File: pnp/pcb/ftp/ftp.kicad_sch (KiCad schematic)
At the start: 84 parts, among them J1 Conn_01x02_Male

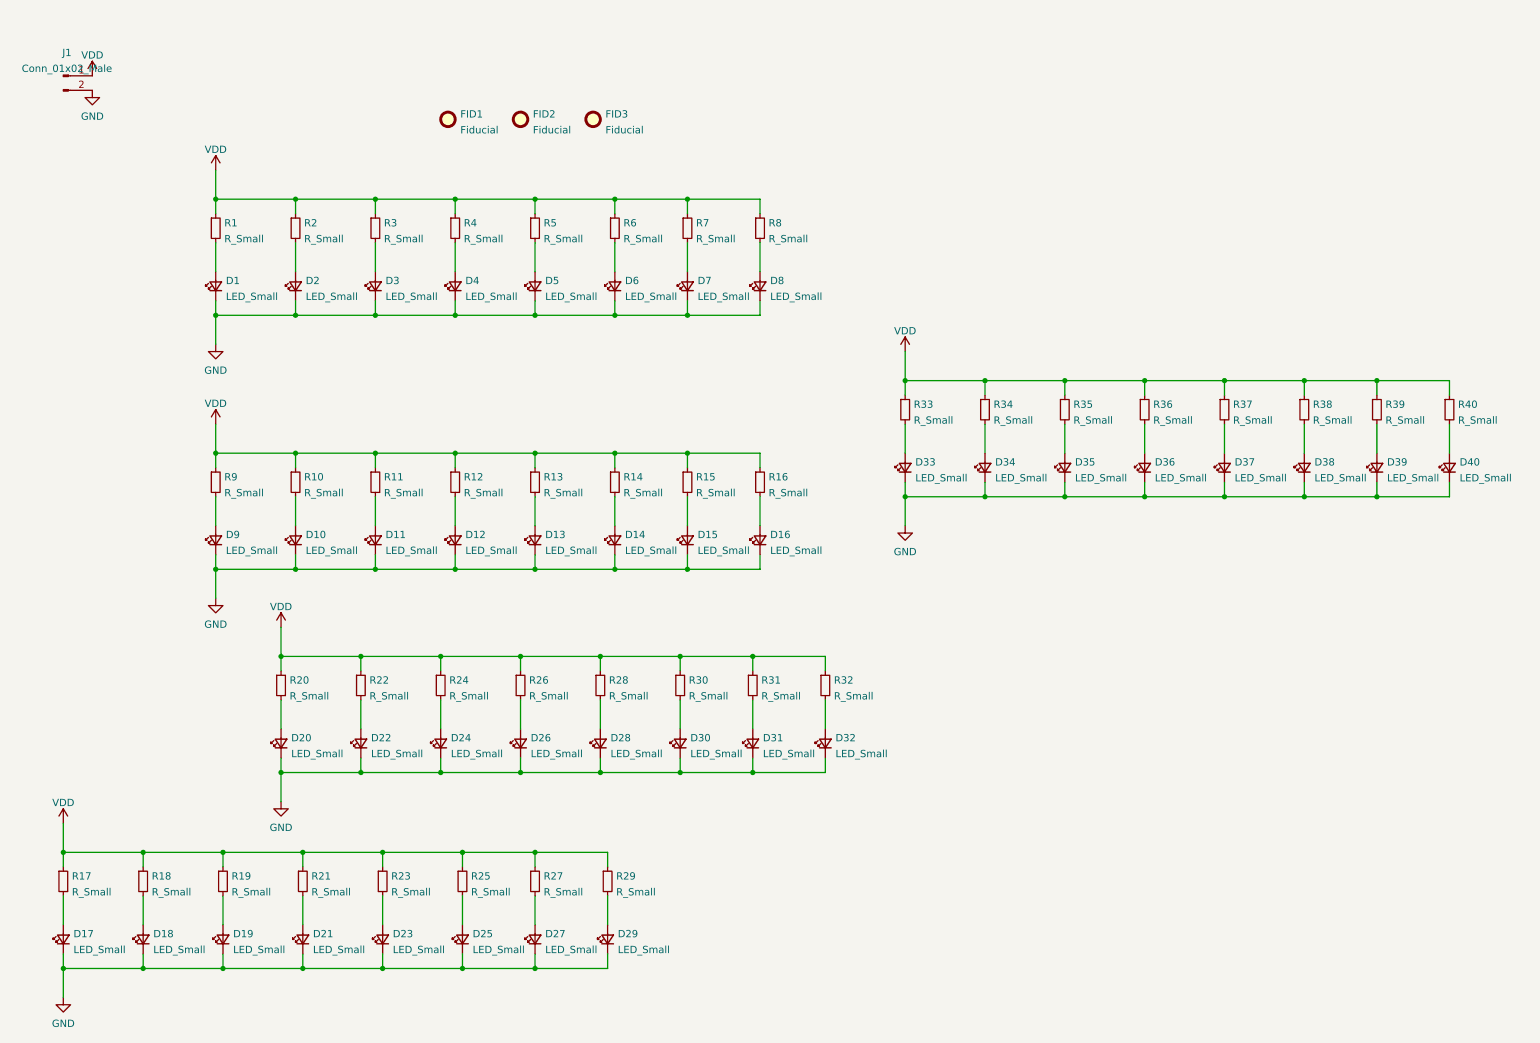
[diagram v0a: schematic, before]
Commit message: Update PCBs to KiCAD 8
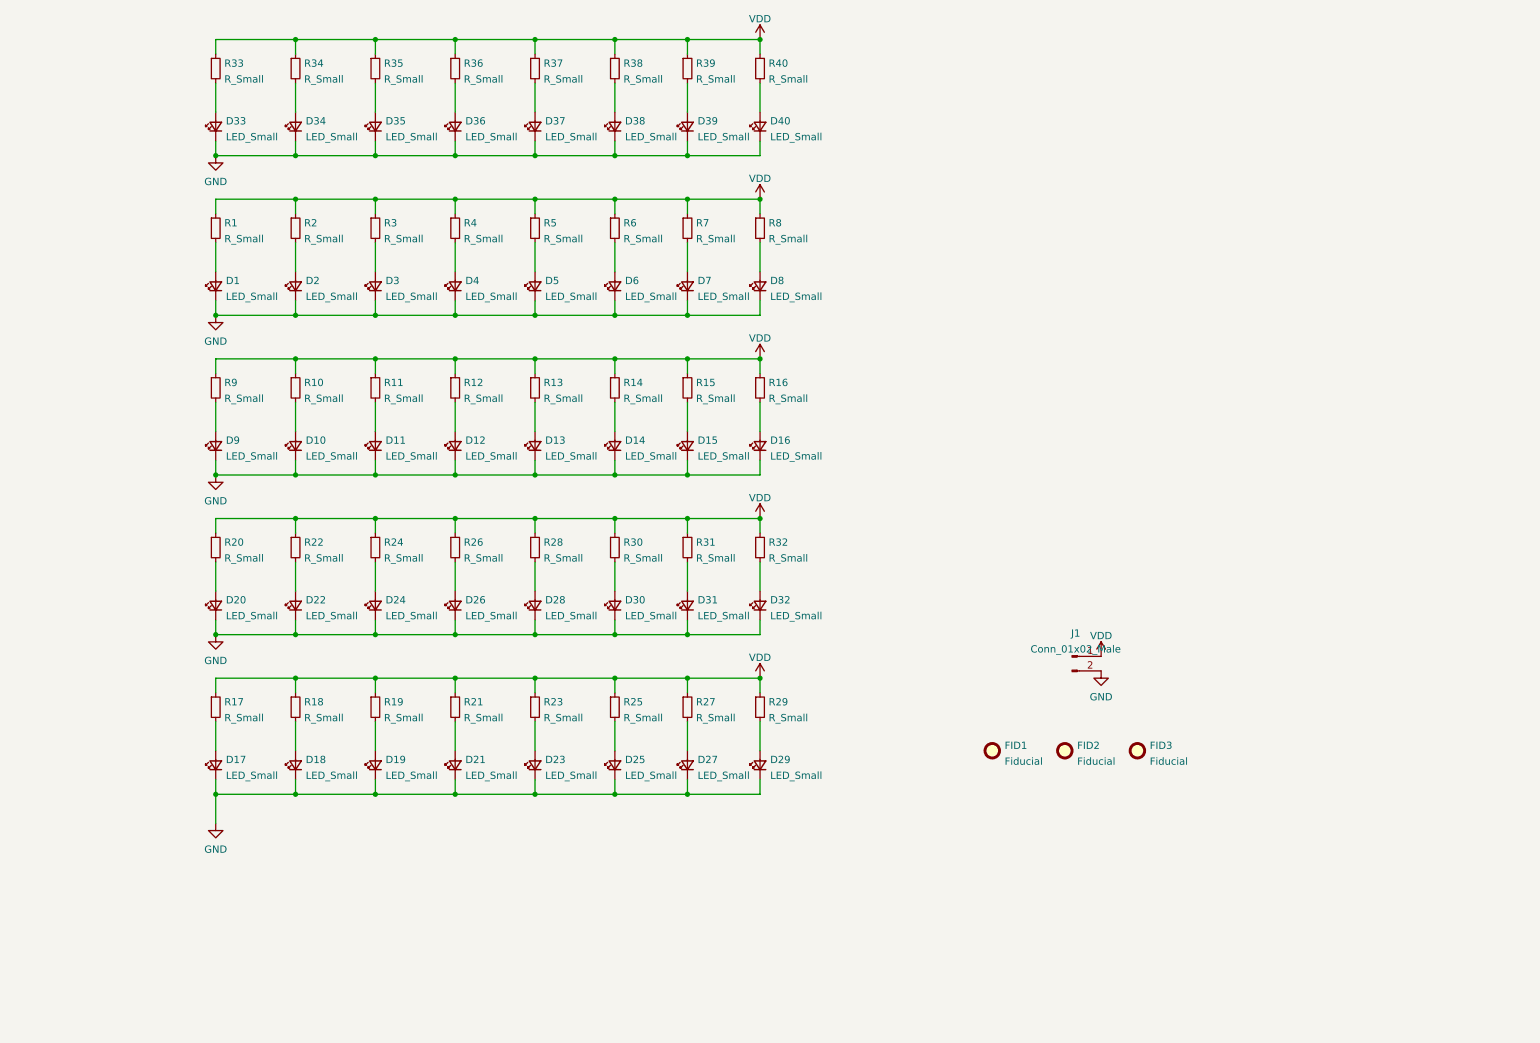
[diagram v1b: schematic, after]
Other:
- moved on the sheet: D10, D11, D12, D13, D14, D15, D16, D17, D18, D19, D20, D21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

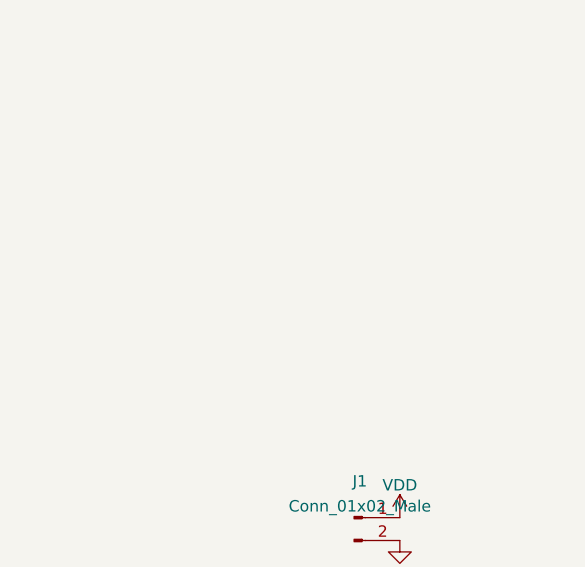
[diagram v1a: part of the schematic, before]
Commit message: Fix mounting holes
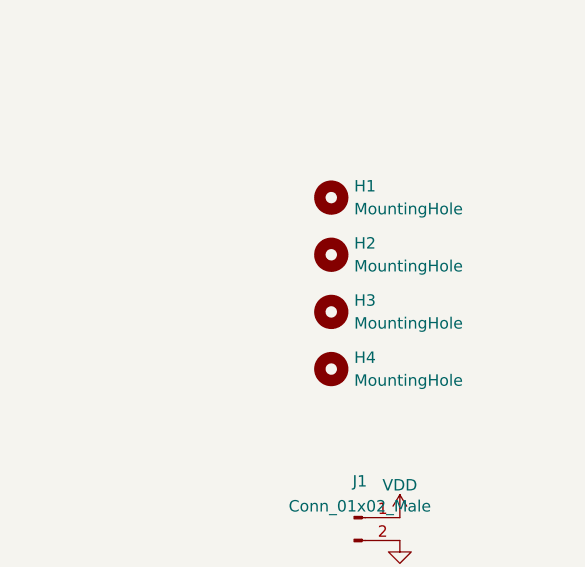
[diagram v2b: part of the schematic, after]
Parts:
- added H1, H2, H3, H4: MountingHole, MountingHole_3.2mm_M3_DIN965_Pad, symbol Mechanical:MountingHole
